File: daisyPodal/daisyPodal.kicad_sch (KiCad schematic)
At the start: 52 parts, among them J1 Guitar in, J2 fsw pin 1, J3 fsw pin 2, J4 fsw pin 4, J5 fsw pin 5, J6 fsw pin 6, J7 Left out, J8 Right out, J9 fsw pin 3, SW1 Switch 1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

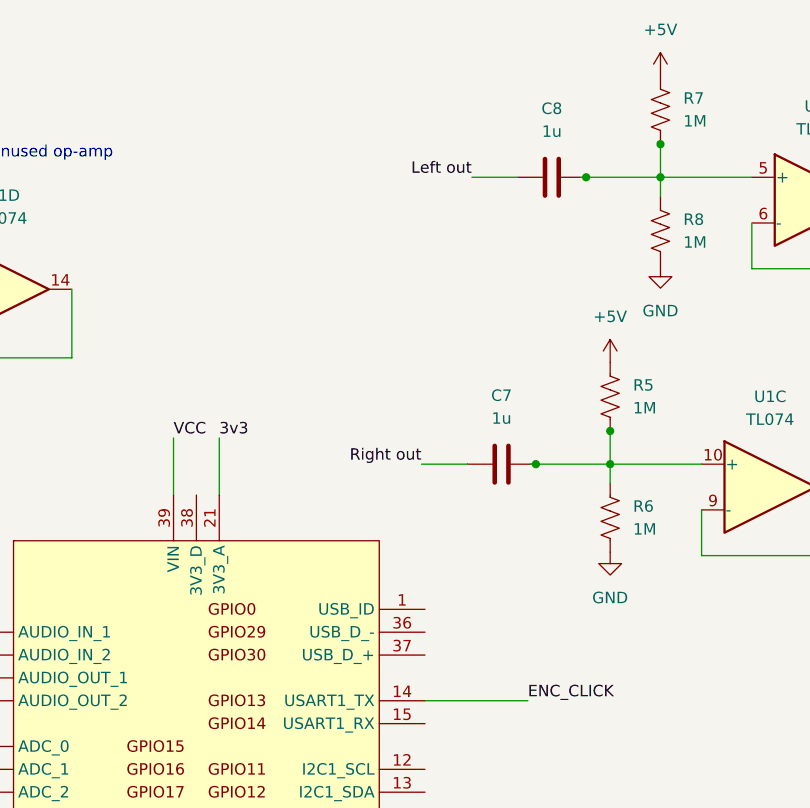
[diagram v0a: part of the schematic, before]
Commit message: Add low pass filters at 22kHz on outputs
Following advice from Daisy forum discussion on Seed rev 7 noise.
Possible to jumper over these if not desired.
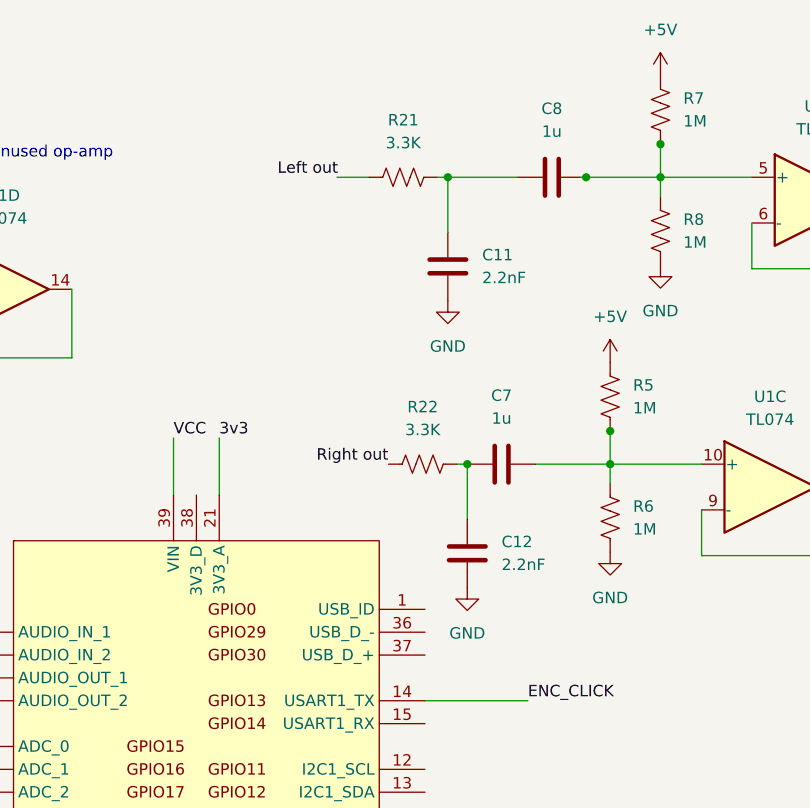
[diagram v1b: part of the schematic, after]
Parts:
- added C11, C12: 2.2nF, Capacitor_THT:C_Rect_L7.0mm_W2.5mm_P5.00mm, symbol Device:C
- added R21, R22: 3.3K, Resistor_THT:R_Axial_DIN0207_L6.3mm_D2.5mm_P10.16mm_Horizontal, symbol Device:R_US
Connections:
- net GND: now also C11.1, C12.1
- net Left out: now also R21.1; no longer C8.1
- net Right out: now also R22.1; no longer C7.1
- new net: C11.2, C8.1, R21.2
- new net: C12.2, C7.1, R22.2
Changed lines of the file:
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@@
   (junction (at 60.96 50.8) (diameter 0) (color 0 0 0 0)
   )
-  (junction (at 200.279 63.881) (diameter 0) (color 0 0 0 0)
-  )
   (junction (at 214.122 32.004) (diameter 0) (color 0 0 0 0)
   )
@@
   (junction (at 74.295 161.29) (diameter 0) (color 0 0 0 0)
   )
+  (junction (at 192.659 63.881) (diameter 0) (color 0 0 0 0)
+  )
   (junction (at 40.767 50.8) (diameter 0) (color 0 0 0 0)
   )
@@
   (junction (at 120.015 161.29) (diameter 0) (color 0 0 0 0)
   )
+  (junction (at 190.5 32.004) (diameter 0) (color 0 0 0 0)
+  )
   (wire (pts (xy 224.282 42.164) (xy 224.282 37.084))
     (stroke (width 0) (type default))
@@
     (stroke (width 0) (type default))
   )
+  (wire (pts (xy 178.181 32.004) (xy 181.737 32.004))
+    (stroke (width 0) (type default))
+  )
   (wire (pts (xy 252.222 34.544) (xy 258.572 34.544))
     (stroke (width 0) (type default))
@@
     (stroke (width 0) (type default))
   )
+  (wire (pts (xy 191.516 63.881) (xy 192.659 63.881))
+    (stroke (width 0) (type default))
+  )
   (wire (pts (xy 18.415 166.37) (xy 18.415 161.29))
     (stroke (width 0) (type default))
@@
     (stroke (width 0) (type default))
   )
+  (wire (pts (xy 189.357 32.004) (xy 190.5 32.004))
+    (stroke (width 0) (type default))
+  )
   (wire (pts (xy 214.122 32.004) (xy 214.122 34.163))
     (stroke (width 0) (type default))
   )
-  (wire (pts (xy 193.167 32.004) (xy 198.247 32.004))
-    (stroke (width 0) (type default))
-  )
   (wire (pts (xy 208.534 60.198) (xy 208.534 63.881))
     (stroke (width 0) (type default))
@@
     (stroke (width 0) (type default))
   )
+  (wire (pts (xy 190.5 32.004) (xy 190.5 38.1))
+    (stroke (width 0) (type default))
+  )
   (wire (pts (xy 127 121.92) (xy 135.255 121.92))
     (stroke (width 0) (type default))
@@
     (stroke (width 0) (type default))
   )
-  (wire (pts (xy 199.644 63.881) (xy 200.279 63.881))
-    (stroke (width 0) (type default))
-  )
   (wire (pts (xy 85.09 110.49) (xy 137.16 110.49))
     (stroke (width 0) (type default))
@@
     (stroke (width 0) (type default))
   )
+  (wire (pts (xy 190.5 32.004) (xy 198.247 32.004))
+    (stroke (width 0) (type default))
+  )
   (wire (pts (xy 100.33 87.63) (xy 100.33 91.44))
     (stroke (width 0) (type default))
@@
     (stroke (width 0) (type default))
   )
+  (wire (pts (xy 192.659 63.881) (xy 192.659 69.977))
+    (stroke (width 0) (type default))
+  )
   (wire (pts (xy 135.255 123.19) (xy 135.255 121.92))
     (stroke (width 0) (type default))
@@
   )
   (wire (pts (xy 61.595 161.29) (xy 61.595 171.45))
-    (stroke (width 0) (type default))
-  )
-  (wire (pts (xy 187.579 63.881) (xy 192.659 63.881))
     (stroke (width 0) (type default))
   )
@@
     (effects (font (size 1.27 1.27)) (justify right bottom))
   )
-  (label "Left out" (at 193.167 32.004 180) (fields_autoplaced)
+  (label "Left out" (at 178.308 32.004 180) (fields_autoplaced)
     (effects (font (size 1.27 1.27)) (justify right bottom))
   )
@@
     (effects (font (size 1.27 1.27)) (justify right bottom))
   )
-  (label "Right out" (at 187.579 63.881 180) (fields_autoplaced)
+  (label "Right out" (at 183.896 63.881 180) (fields_autoplaced)
     (effects (font (size 1.27 1.27)) (justify right bottom))
   )
@@
         (path "/12e895f7-e5ae-4934-aed6-e6e04c63dd03"
           (reference "#PWR027") (unit 1)
+        )
+      )
+    )
+  )
+  (symbol (lib_id "power:GND") (at 192.659 77.597 0) (unit 1)
+    (in_bom yes) (on_board yes) (dnp no) (fields_autoplaced)
+    (property "Reference" "#PWR032" (at 192.659 83.947 0)
+      (effects (font (size 1.27 1.27)) hide)
+    )
+    (property "Value" "GND" (at 192.659 82.677 0)
+      (effects (font (size 1.27 1.27)))
+    )
+    (property "Footprint" "" (at 192.659 77.597 0)
+      (effects (font (size 1.27 1.27)) hide)
+    )
+    (property "Datasheet" "" (at 192.659 77.597 0)
+      (effects (font (size 1.27 1.27)) hide)
+    )
+    (pin "1")
+    (instances
+      (project "daisyPodal"
+        (path "/12e895f7-e5ae-4934-aed6-e6e04c63dd03"
+          (reference "#PWR032") (unit 1)
         )
       )
@@
         (path "/12e895f7-e5ae-4934-aed6-e6e04c63dd03"
           (reference "C3") (unit 1)
+        )
+      )
+    )
+  )
+  (symbol (lib_id "Device:R_US") (at 187.706 63.881 90) (unit 1)
+    (in_bom yes) (on_board yes) (dnp no)
+    (property "Reference" "R22" (at 187.706 57.531 90)
+      (effects (font (size 1.27 1.27)))
+    )
+    (property "Value" "3.3K" (at 187.706 60.071 90)
+      (effects (font (size 1.27 1.27)))
+    )
+    (property "Footprint" "Resistor_THT:R_Axial_DIN0207_L6.3mm_D2.5mm_P10.16mm_Horizontal" (at 187.96 62.865 90)
+      (effects (font (size 1.27 1.27)) hide)
+    )
+    (property "Datasheet" "~" (at 187.706 63.881 0)
+      (effects (font (size 1.27 1.27)) hide)
+    )
+    (pin "1")
+    (pin "2")
+    (instances
+      (project "daisyPodal"
+        (path "/12e895f7-e5ae-4934-aed6-e6e04c63dd03"
+          (reference "R22") (unit 1)
         )
       )
@@
     )
   )
+  (symbol (lib_id "power:GND") (at 190.5 45.72 0) (unit 1)
+    (in_bom yes) (on_board yes) (dnp no) (fields_autoplaced)
+    (property "Reference" "#PWR031" (at 190.5 52.07 0)
+      (effects (font (size 1.27 1.27)) hide)
+    )
+    (property "Value" "GND" (at 190.5 50.8 0)
+      (effects (font (size 1.27 1.27)))
+    )
+    (property "Footprint" "" (at 190.5 45.72 0)
+      (effects (font (size 1.27 1.27)) hide)
+    )
+    (property "Datasheet" "" (at 190.5 45.72 0)
+      (effects (font (size 1.27 1.27)) hide)
+    )
+    (pin "1")
+    (instances
+      (project "daisyPodal"
+        (path "/12e895f7-e5ae-4934-aed6-e6e04c63dd03"
+          (reference "#PWR031") (unit 1)
+        )
+      )
+    )
+  )
   (symbol (lib_id "power:GND") (at 81.28 101.6 180) (unit 1)
     (in_bom yes) (on_board yes) (dnp no) (fields_autoplaced)
@@
     )
   )
+  (symbol (lib_id "Device:C") (at 192.659 73.787 180) (unit 1)
+    (in_bom yes) (on_board yes) (dnp no) (fields_autoplaced)
+    (property "Reference" "C12" (at 196.469 72.517 0)
+      (effects (font (size 1.27 1.27)) (justify right))
+    )
+    (property "Value" "2.2nF" (at 196.469 75.057 0)
+      (effects (font (size 1.27 1.27)) (justify right))
+    )
+    (property "Footprint" "Capacitor_THT:C_Rect_L7.0mm_W2.5mm_P5.00mm" (at 191.6938 69.977 0)
+      (effects (font (size 1.27 1.27)) hide)
+    )
+    (property "Datasheet" "~" (at 192.659 73.787 0)
+      (effects (font (size 1.27 1.27)) hide)
+    )
+    (pin "1")
+    (pin "2")
+    (instances
+      (project "daisyPodal"
+        (path "/12e895f7-e5ae-4934-aed6-e6e04c63dd03"
+          (reference "C12") (unit 1)
+        )
+      )
+    )
+  )
   (symbol (lib_id "Device:R_US") (at 215.011 157.099 90) (unit 1)
     (in_bom yes) (on_board yes) (dnp no)
@@
     )
   )
+  (symbol (lib_id "Device:C") (at 190.5 41.91 180) (unit 1)
+    (in_bom yes) (on_board yes) (dnp no) (fields_autoplaced)
+    (property "Reference" "C11" (at 194.31 40.64 0)
+      (effects (font (size 1.27 1.27)) (justify right))
+    )
+    (property "Value" "2.2nF" (at 194.31 43.18 0)
+      (effects (font (size 1.27 1.27)) (justify right))
+    )
+    (property "Footprint" "Capacitor_THT:C_Rect_L7.0mm_W2.5mm_P5.00mm" (at 189.5348 38.1 0)
+      (effects (font (size 1.27 1.27)) hide)
+    )
+    (property "Datasheet" "~" (at 190.5 41.91 0)
+      (effects (font (size 1.27 1.27)) hide)
+    )
+    (pin "1")
+    (pin "2")
+    (instances
+      (project "daisyPodal"
+        (path "/12e895f7-e5ae-4934-aed6-e6e04c63dd03"
+          (reference "C11") (unit 1)
+        )
+      )
+    )
+  )
   (symbol (lib_id "power:GND") (at 60.96 71.12 0) (unit 1)
     (in_bom yes) (on_board yes) (dnp no) (fields_autoplaced)
@@
         )
       )
+    )
+  )
+  (symbol (lib_id "Device:R_US") (at 185.547 32.004 90) (unit 1)
+    (in_bom yes) (on_board yes) (dnp no)
+    (property "Reference" "R21" (at 185.547 25.654 90)
+      (effects (font (size 1.27 1.27)))
+    )
+    (property "Value" "3.3K" (at 185.547 28.194 90)
+      (effects (font (size 1.27 1.27)))
+    )
+    (property "Footprint" "Resistor_THT:R_Axial_DIN0207_L6.3mm_D2.5mm_P10.16mm_Horizontal" (at 185.801 30.988 90)
+      (effects (font (size 1.27 1.27)) hide)
+    )
+    (property "Datasheet" "~" (at 185.547 32.004 0)
+      (effects (font (size 1.27 1.27)) hide)
+    )
+    (pin "1")
+    (pin "2")
+    (instances
+      (project "daisyPodal"
+        (path "/12e895f7-e5ae-4934-aed6-e6e04c63dd03"
+          (reference "R21") (unit 1)
+        )
+      )

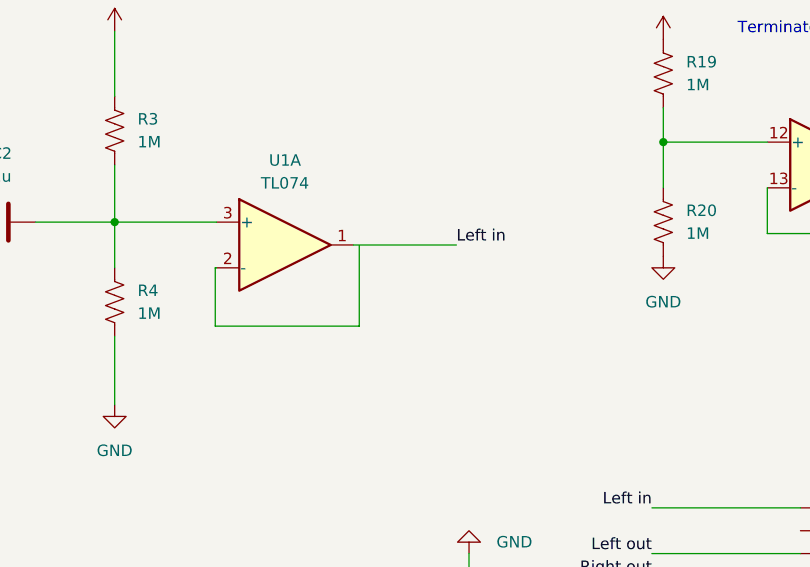
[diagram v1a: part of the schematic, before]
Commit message: Fix missing connection in schematic on input stage
Means a jumper needed between pins 1 and 2 of TL074
on board v0.2
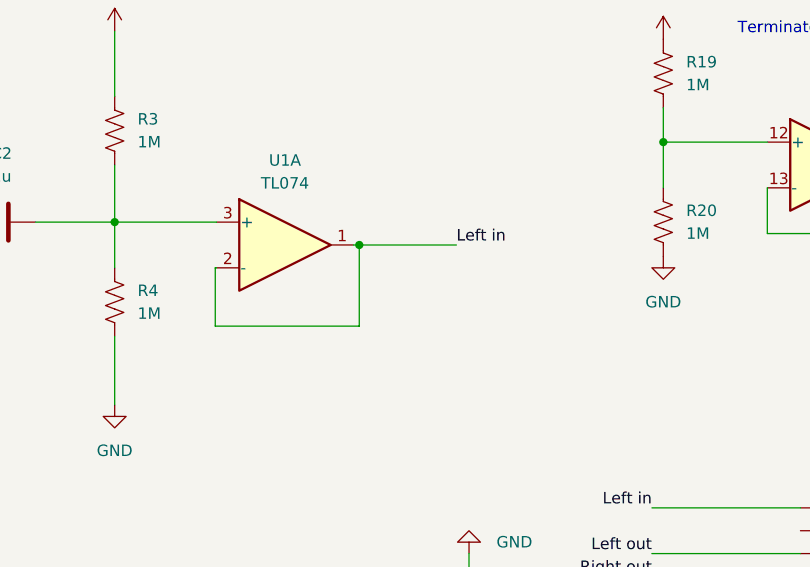
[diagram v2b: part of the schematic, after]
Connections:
- net Left in: now also U1.2 (-)
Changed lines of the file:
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@@
   (junction (at 214.122 28.321) (diameter 0) (color 0 0 0 0)
   )
+  (junction (at 88.138 53.34) (diameter 0) (color 0 0 0 0)
+  )
   (junction (at 208.534 60.198) (diameter 0) (color 0 0 0 0)
   )
@@
     (stroke (width 0) (type default))
   )
-  (wire (pts (xy 87.503 53.34) (xy 98.933 53.34))
+  (wire (pts (xy 87.503 53.34) (xy 88.138 53.34))
     (stroke (width 0) (type default))
   )
@@
     (stroke (width 0) (type default))
   )
+  (wire (pts (xy 88.138 53.34) (xy 98.933 53.34))
+    (stroke (width 0) (type default))
+  )
   (wire (pts (xy 165.1 60.96) (xy 165.1 67.31))
     (stroke (width 0) (type default))
@@
     (stroke (width 0) (type default))
   )
-  (wire (pts (xy 88.138 53.467) (xy 88.138 62.357))
-    (stroke (width 0) (type default))
-  )
+  (wire (pts (xy 88.138 53.34) (xy 88.138 62.357))
+    (stroke (width 0) (type default))
+  )
